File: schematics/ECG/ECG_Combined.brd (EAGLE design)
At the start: 27.3 x 27.3 mm, 71 parts, among them IC1 ADS1293, IC2 LIS3DH, IC3 MCP1703, IC4 CC2541, IC5 FSA4157, IC6 FSA4157, IC7 FSA4157, X1 XTAL-2SMD, X2 XTAL_403, X3 XTAL-CSM7

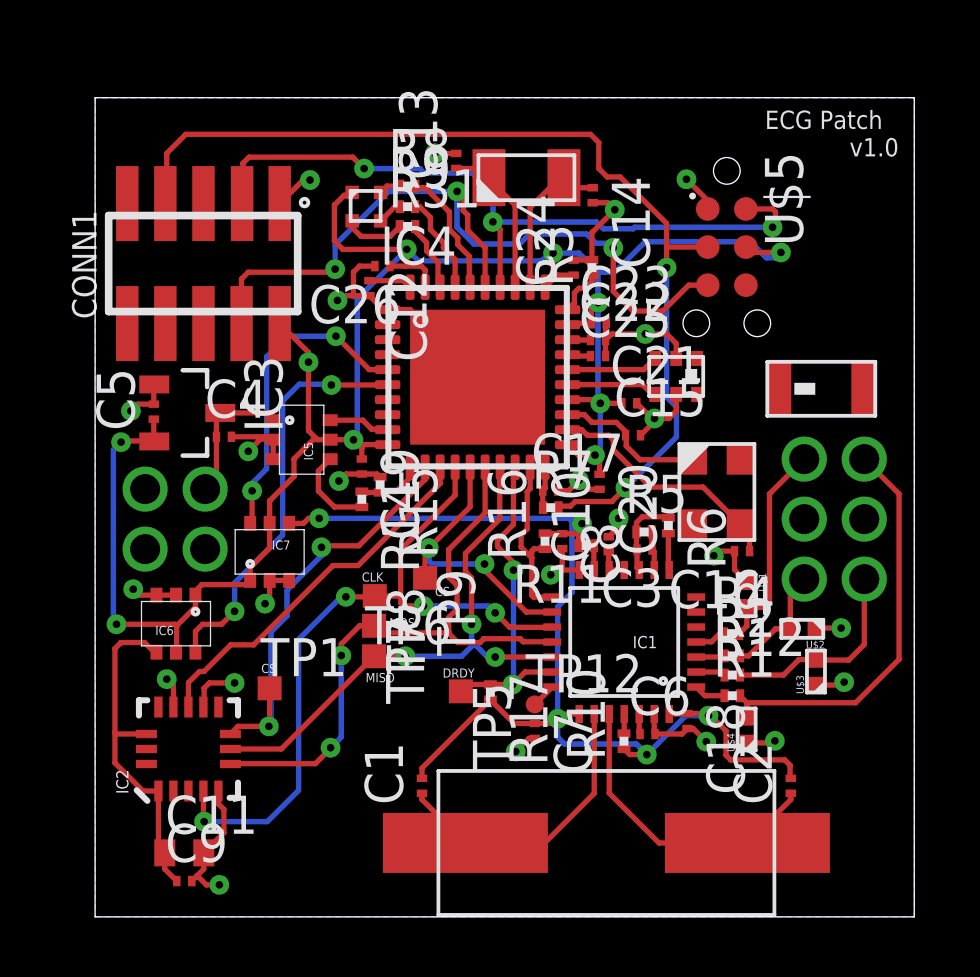
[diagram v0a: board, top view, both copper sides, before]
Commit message: added TP to ALARMB pin
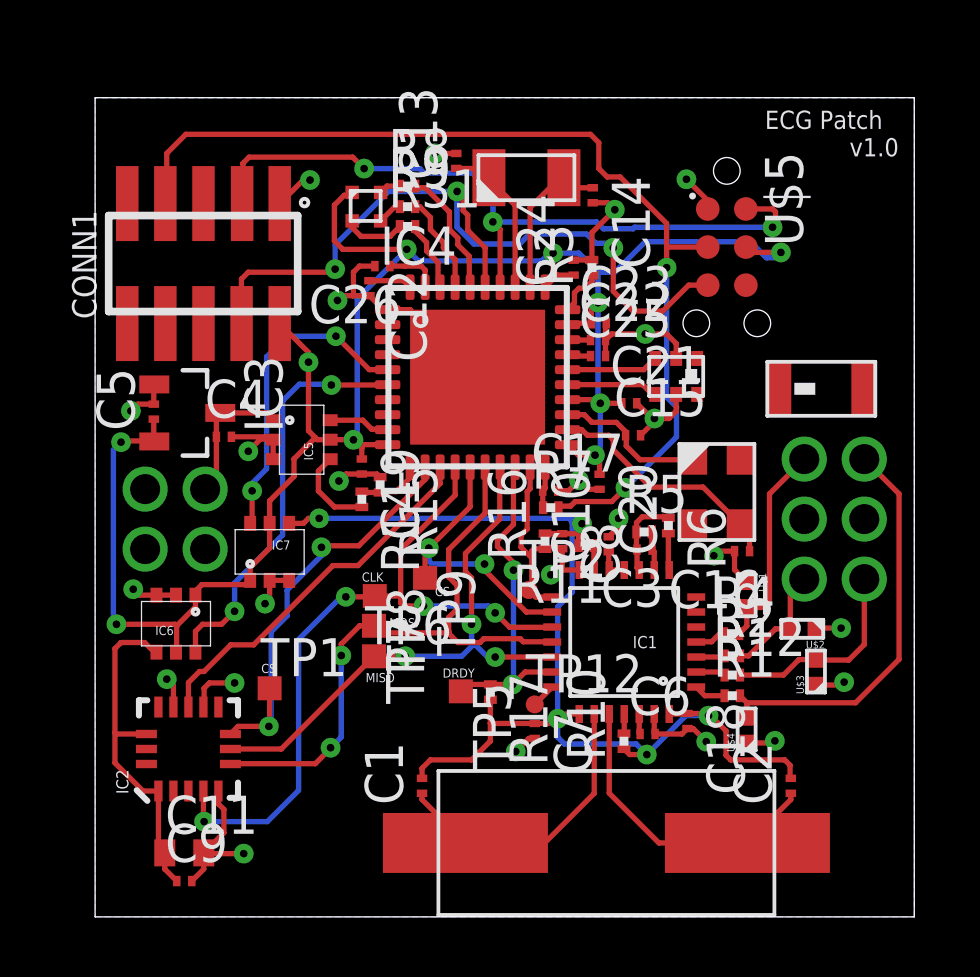
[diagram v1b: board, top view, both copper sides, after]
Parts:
- added TP2: TPSTP06R, testpad:TP06R
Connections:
- net ALARMB: now also TP2.TP
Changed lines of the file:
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@@
 <attribute name="TP_SIGNAL_NAME" value="" x="5.8166" y="7.62" size="0.3048" layer="27" display="off"/>
+</element>
+<element name="TP2" library="testpad" package="TP06R" value="TPSTP06R" x="14.4526" y="10.8966">
+<attribute name="TP_SIGNAL_NAME" value="" x="14.4526" y="10.8966" size="1.778" layer="27" display="off"/>
 </element>
 </elements>
@@
 <via x="4.6482" y="7.7978" extent="1-16" drill="0.254"/>
 <via x="2.3876" y="7.9248" extent="1-16" drill="0.254"/>
-<via x="4.1402" y="1.0668" extent="1-16" drill="0.254"/>
+<via x="4.953" y="2.1082" extent="1-16" drill="0.254"/>
 <via x="16.129" y="14.5542" extent="1-16" drill="0.254"/>
 <wire x1="2.0456" y1="10.7234" x2="1.4686" y2="10.7234" width="0.1778" layer="1"/>
@@
 <wire x1="4.2926" y1="2.8044" x2="3.6218" y2="2.1336" width="0.1778" layer="1"/>
 <wire x1="3.6218" y1="2.1336" x2="3.6218" y2="1.5938" width="0.1778" layer="1"/>
-<wire x1="3.6218" y1="1.5938" x2="3.4016" y2="1.3736" width="0.1778" layer="1"/>
-<wire x1="3.4016" y1="1.3736" x2="3.2218" y2="1.1938" width="0.1778" layer="1"/>
+<wire x1="3.6218" y1="1.5938" x2="3.2218" y2="1.1938" width="0.1778" layer="1"/>
 <wire x1="4.6482" y1="7.7978" x2="3.81" y2="7.7978" width="0.1778" layer="1"/>
 <wire x1="3.81" y1="7.7978" x2="3.6322" y2="7.62" width="0.1778" layer="1"/>
@@
 <wire x1="7.1628" y1="24.5618" x2="6.9364" y2="24.5618" width="0.1778" layer="1"/>
 <wire x1="6.9364" y1="24.5618" x2="6.1516" y2="23.777" width="0.1778" layer="1"/>
-<wire x1="4.1402" y1="1.0668" x2="3.7084" y2="1.0668" width="0.1778" layer="1"/>
-<wire x1="3.7084" y1="1.0668" x2="3.4016" y2="1.3736" width="0.1778" layer="1"/>
 <wire x1="5.8174" y1="11.2166" x2="6.4674" y2="11.2166" width="0.1778" layer="1"/>
 <wire x1="6.4776" y1="11.2268" x2="6.4674" y2="11.2166" width="0.1778" layer="1"/>
@@
 <wire x1="21.717" y1="5.7976" x2="22.587" y2="5.7976" width="0.1778" layer="1"/>
 <wire x1="22.587" y1="5.7976" x2="22.6568" y2="5.8674" width="0.1778" layer="1"/>
+<wire x1="4.953" y1="2.1082" x2="3.6472" y2="2.1082" width="0.1778" layer="1"/>
+<wire x1="3.6472" y1="2.1082" x2="3.6218" y2="2.1336" width="0.1778" layer="1"/>
 </signal>
 <signal name="IN1">
@@
 <wire x1="14.6304" y1="12.2682" x2="14.9974" y2="12.2682" width="0.1778" layer="1"/>
 <wire x1="14.9974" y1="12.2682" x2="14.998" y2="12.2676" width="0.1778" layer="1"/>
-<wire x1="15.2364" y1="10.6618" x2="14.6112" y2="10.6618" width="0.1778" layer="1"/>
-<wire x1="14.6112" y1="10.6618" x2="14.5542" y2="10.7188" width="0.1778" layer="1"/>
-<wire x1="14.5542" y1="10.7188" x2="14.5542" y2="11.9634" width="0.1778" layer="1"/>
 <wire x1="14.5542" y1="11.9634" x2="14.5542" y2="12.192" width="0.1778" layer="1"/>
 <wire x1="14.5542" y1="12.192" x2="14.6304" y2="12.2682" width="0.1778" layer="1"/>
@@
 <wire x1="14.1986" y1="12.7254" x2="14.1986" y2="12.319" width="0.1778" layer="1"/>
 <wire x1="14.1986" y1="12.319" x2="14.5542" y2="11.9634" width="0.1778" layer="1"/>
+<contactref element="TP2" pad="TP"/>
+<wire x1="14.5542" y1="11.9634" x2="14.5542" y2="10.9982" width="0.1778" layer="1"/>
+<wire x1="14.5542" y1="10.9982" x2="14.4526" y2="10.8966" width="0.1778" layer="1"/>
+<wire x1="15.2364" y1="10.6618" x2="14.6874" y2="10.6618" width="0.1778" layer="1"/>
+<wire x1="14.6874" y1="10.6618" x2="14.4526" y2="10.8966" width="0.1778" layer="1"/>
 </signal>
 <signal name="LA">
@@
 <wire x1="14.6558" y1="6.4476" x2="15.2614" y2="6.4476" width="0.1778" layer="1"/>
 <wire x1="15.2614" y1="6.4476" x2="15.4178" y2="6.604" width="0.1778" layer="1"/>
-<wire x1="14.6558" y1="6.4476" x2="13.9644" y2="6.4476" width="0.1778" layer="1"/>
-<wire x1="13.9644" y1="6.4476" x2="13.1744" y2="7.2376" width="0.1778" layer="1"/>
-<wire x1="10.8966" y1="4.6188" x2="10.8966" y2="4.9598" width="0.1778" layer="1"/>
-<wire x1="10.8966" y1="4.9598" x2="13.1744" y2="7.2376" width="0.1778" layer="1"/>
 <wire x1="21.1836" y1="5.2324" x2="22.987" y2="5.2324" width="0.1778" layer="1"/>
 <wire x1="22.987" y1="5.2324" x2="23.1648" y2="5.0546" width="0.1778" layer="1"/>
@@
 <wire x1="21.0312" y1="6.1976" x2="21.0312" y2="5.3848" width="0.1778" layer="1"/>
 <wire x1="21.0312" y1="5.3848" x2="21.1836" y2="5.2324" width="0.1778" layer="1"/>
+<wire x1="13.1744" y1="7.2376" x2="13.1744" y2="6.4516" width="0.1778" layer="1"/>
+<wire x1="13.1744" y1="6.4516" x2="13.1744" y2="5.8592" width="0.1778" layer="1"/>
+<wire x1="13.1744" y1="5.8592" x2="12.5476" y2="5.2324" width="0.1778" layer="1"/>
+<wire x1="12.5476" y1="5.2324" x2="11.176" y2="5.2324" width="0.1778" layer="1"/>
+<wire x1="11.176" y1="5.2324" x2="10.8966" y2="4.953" width="0.1778" layer="1"/>
+<wire x1="10.8966" y1="4.953" x2="10.8966" y2="4.6188" width="0.1778" layer="1"/>
+<wire x1="14.6558" y1="6.4476" x2="13.1784" y2="6.4476" width="0.1778" layer="1"/>
+<wire x1="13.1784" y1="6.4476" x2="13.1744" y2="6.4516" width="0.1778" layer="1"/>
 </signal>
 <signal name="BLUE_LED">

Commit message: added 50ohm antenna trace. renamed TVS components
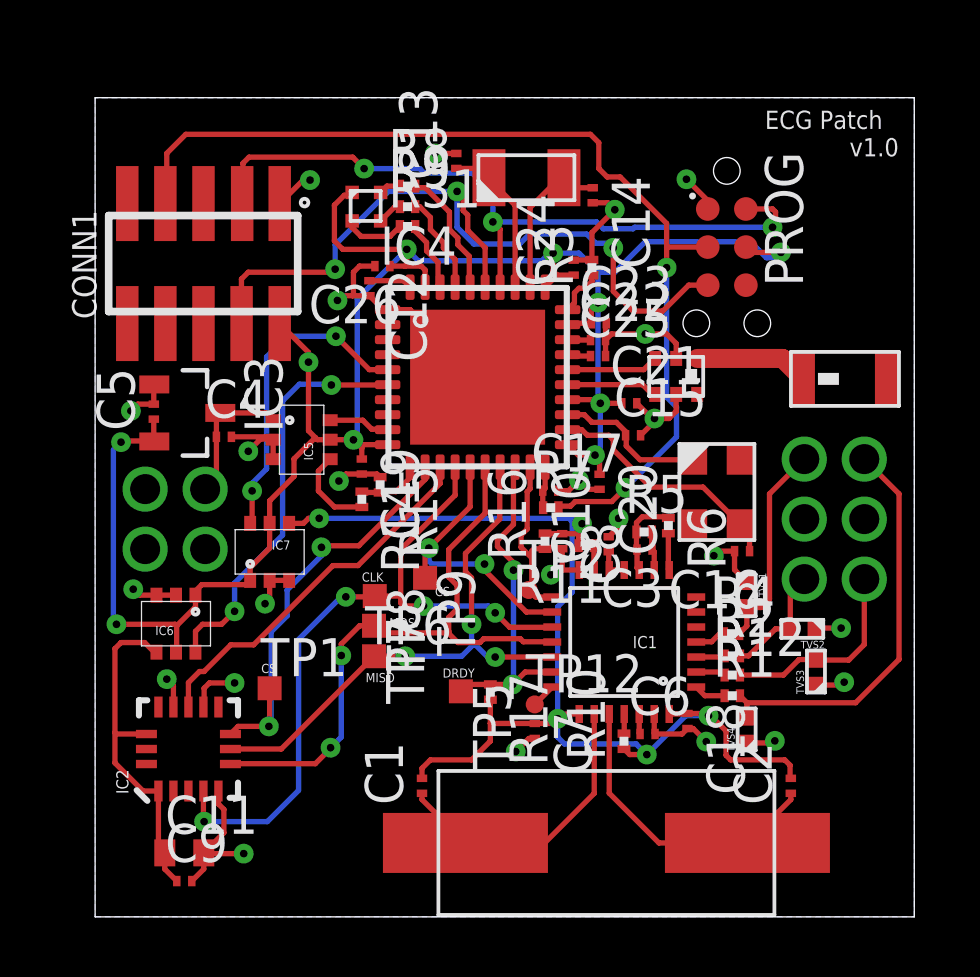
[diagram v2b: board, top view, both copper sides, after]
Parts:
- C26: value 1.0uF -> 1uF
- moved RF 0.85 mm to (25.1, 17.9)
- renumbered U$1 to TVS1, U$2 to TVS2, U$3 to TVS3, U$4 to TVS4, U$5 to PROG
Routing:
- net N$6: track 0.00 -> 3.81 mm
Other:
- board text removed: "TO-DO: Calculate trace width for 50ohm impedence"
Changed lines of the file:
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@@
 <setting verticaltext="up"/>
 </settings>
-<grid distance="1" unitdist="mil" unit="mil" style="lines" multiple="1" display="yes" altdistance="0.025" altunitdist="inch" altunit="inch"/>
+<grid distance="1" unitdist="mil" unit="mm" style="lines" multiple="1" display="yes" altdistance="0.025" altunitdist="inch" altunit="inch"/>
 <layers>
 <layer number="1" name="Top" color="4" fill="1" visible="yes" active="yes"/>
@@
 <text x="5.5372" y="8.128" size="0.3048" layer="21">CS</text>
 <text x="11.3284" y="10.6934" size="0.3048" layer="21">CS</text>
-<text x="0.1016" y="27.9908" size="0.3048" layer="48">TO-DO: Calculate trace width for 50ohm impedence</text>
 </plain>
 <attributes>
@@
 <element name="C24" library="rcl" package="C0201" value="0.1uF" x="15.9512" y="21.6408" rot="R90"/>
 <element name="C25" library="rcl" package="C0201" value="220pF" x="16.764" y="18.6944"/>
-<element name="C26" library="rcl" package="C0201" value="1.0uF" x="9.5758" y="21.6916" rot="R180"/>
+<element name="C26" library="rcl" package="C0201" value="1uF" x="9.5758" y="21.6916" rot="R180"/>
 <element name="IC7" library="fairchild" package="SC70-6" value="FSA4157" x="5.8674" y="12.1666"/>
 <element name="R8" library="rcl" package="R0201" value="1K" x="10.414" y="24.3586"/>
@@
 <element name="R9" library="rcl" package="R0201" value="1K" x="10.414" y="23.6728"/>
 <element name="CONN2" library="harwin" package="M80-4-V" value="M80-4V" x="2.667" y="13.2588" rot="R180"/>
-<element name="U$1" library="semtech" package="0402" value="ZD_0402" x="21.717" y="10.7188" rot="R270"/>
-<element name="U$2" library="semtech" package="0402" value="ZD_0402" x="23.5712" y="9.6012" rot="R180"/>
-<element name="U$3" library="semtech" package="0402" value="ZD_0402" x="24.0284" y="8.1788" rot="R90"/>
-<element name="U$4" library="semtech" package="0402" value="ZD_0402" x="21.717" y="6.2484" rot="R90"/>
-<element name="RF" library="johanson" package="ANTENNA_SMD" value="ANTENNA_SMD" x="24.2824" y="17.6022" rot="R180"/>
+<element name="TVS1" library="semtech" package="0402" value="ZD_0402" x="21.717" y="10.7188" rot="R270"/>
+<element name="TVS2" library="semtech" package="0402" value="ZD_0402" x="23.5712" y="9.6012" rot="R180"/>
+<element name="TVS3" library="semtech" package="0402" value="ZD_0402" x="24.0284" y="8.1788" rot="R90"/>
+<element name="TVS4" library="semtech" package="0402" value="ZD_0402" x="21.717" y="6.2484" rot="R90"/>
+<element name="RF" library="johanson" package="ANTENNA_SMD" value="ANTENNA_SMD" x="25.0698" y="17.9324" rot="R180"/>
 <element name="IC8" library="johanson" package="BALUN_SMD_2450BM_SERIES" value="" x="19.304" y="17.9832"/>
-<element name="U$5" library="tagconnect" package="TC2030-MCP-NL" value="TC2030-MCP-NL" x="21.0566" y="24.8666" rot="R270"/>
+<element name="PROG" library="tagconnect" package="TC2030-MCP-NL" value="TC2030-MCP-NL" x="21.0566" y="24.8666" rot="R270"/>
 <element name="TP1" library="testpad" package="TP08SQ" value="TPSTP08SQ" x="5.8166" y="7.62">
 <attribute name="TP_SIGNAL_NAME" value="" x="5.8166" y="7.62" size="0.3048" layer="27" display="off"/>
@@
 <contactref element="IC7" pad="2"/>
 <contactref element="CONN2" pad="2"/>
-<contactref element="U$4" pad="1"/>
-<contactref element="U$3" pad="1"/>
-<contactref element="U$2" pad="1"/>
-<contactref element="U$1" pad="1"/>
+<contactref element="TVS4" pad="1"/>
+<contactref element="TVS3" pad="1"/>
+<contactref element="TVS2" pad="1"/>
+<contactref element="TVS1" pad="1"/>
 <contactref element="IC8" pad="5"/>
 <contactref element="IC8" pad="6"/>
@@
 <wire x1="18.5634" y1="16.6116" x2="18.5634" y2="16.4338" width="0.1778" layer="1"/>
 <wire x1="18.5634" y1="16.4338" x2="18.1824" y2="16.0528" width="0.1778" layer="1"/>
-<contactref element="U$5" pad="1"/>
+<contactref element="PROG" pad="1"/>
 <wire x1="8.6106" y1="20.7304" x2="8.5852" y2="20.705" width="0.1778" layer="1"/>
 <wire x1="8.2336" y1="20.705" x2="8.0772" y2="20.5486" width="0.1778" layer="1"/>
@@
 <signal name="RA">
 <contactref element="R1" pad="2"/>
-<contactref element="U$4" pad="2"/>
+<contactref element="TVS4" pad="2"/>
 <wire x1="21.7242" y1="6.6548" x2="21.717" y2="6.6476" width="0.1778" layer="1"/>
 <wire x1="21.7242" y1="6.6548" x2="21.7242" y2="7.141" width="0.1778" layer="1"/>
@@
 <signal name="LL">
 <contactref element="R2" pad="2"/>
-<contactref element="U$2" pad="2"/>
+<contactref element="TVS2" pad="2"/>
 <contactref element="CONN3" pad="6"/>
 <wire x1="23.172" y1="9.6012" x2="23.172" y2="10.7928" width="0.1778" layer="1"/>
@@
 <signal name="RL">
 <contactref element="R4" pad="2"/>
-<contactref element="U$1" pad="2"/>
+<contactref element="TVS1" pad="2"/>
 <wire x1="22.479" y1="14.0998" x2="22.479" y2="10.5918" width="0.1778" layer="1"/>
 <wire x1="22.479" y1="10.5918" x2="22.1996" y2="10.3124" width="0.1778" layer="1"/>
@@
 <wire x1="16.7198" y1="17.24" x2="16.8402" y2="17.1196" width="0.1778" layer="1"/>
 <wire x1="16.8402" y1="17.1196" x2="17.5554" y2="17.1196" width="0.1778" layer="1"/>
-<contactref element="U$5" pad="4"/>
+<contactref element="PROG" pad="4"/>
 <via x="16.6624" y="15.3924" extent="1-16" drill="0.254"/>
 <via x="8.6106" y="15.9004" extent="1-16" drill="0.254"/>
@@
 <contactref element="R7" pad="2"/>
 <contactref element="CONN1" pad="7"/>
-<contactref element="U$5" pad="3"/>
+<contactref element="PROG" pad="3"/>
 <wire x1="20.4216" y1="22.3266" x2="19.0754" y2="22.3266" width="0.1778" layer="1"/>
 <via x="19.05" y="21.6408" extent="1-16" drill="0.254"/>
@@
 <wire x1="13.2588" y1="24.1046" x2="13.2588" y2="23.1648" width="0.1778" layer="16"/>
 <via x="8.9662" y="24.9428" extent="1-16" drill="0.254"/>
-<contactref element="U$5" pad="2"/>
+<contactref element="PROG" pad="2"/>
 <wire x1="10.9728" y1="24.7904" x2="12.573" y2="24.7904" width="0.1778" layer="16"/>
 <wire x1="12.573" y1="24.7904" x2="13.2588" y2="24.1046" width="0.1778" layer="16"/>
@@
 <wire x1="12.9998" y1="20.99" x2="12.9998" y2="22.3062" width="0.1778" layer="1"/>
 <wire x1="12.9998" y1="22.3062" x2="12.4206" y2="22.8854" width="0.1778" layer="1"/>
-<contactref element="U$5" pad="5"/>
+<contactref element="PROG" pad="5"/>
 <wire x1="12.4206" y1="22.8854" x2="12.4206" y2="23.3934" width="0.1778" layer="1"/>
 <wire x1="12.4206" y1="23.3934" x2="12.2682" y2="23.5458" width="0.1778" layer="1"/>
@@
 <signal name="LA">
 <contactref element="R12" pad="2"/>
-<contactref element="U$3" pad="2"/>
+<contactref element="TVS3" pad="2"/>
 <contactref element="CONN3" pad="1"/>
 <wire x1="25.638" y1="11.2588" x2="25.638" y2="9.0772" width="0.1778" layer="1"/>
@@
 <contactref element="IC8" pad="1"/>
 <contactref element="RF" pad="1"/>
-<wire x1="22.8064" y1="17.6022" x2="20.069" y2="18.6142" width="0" layer="19" extent="1-1"/>
+<wire x1="20.069" y1="18.6142" x2="22.912" y2="18.6142" width="0.635" layer="1"/>
+<wire x1="22.912" y1="18.6142" x2="23.5938" y2="17.9324" width="0.635" layer="1"/>
 </signal>
 <signal name="N/C">
